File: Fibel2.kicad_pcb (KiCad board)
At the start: 2 copper layers, 210 x 148 mm, 315 parts, among them J1201 Orin Nano, J301 Conn_01x02, J302 Conn_01x02, J303 Conn_01x02, J702 SPK_JST_L, J703 SPK_JST_R, J704 Conn_02x20_Odd_Even, J801 Conn_02x20_Odd_Even, Q301 CSD17581Q3A, Q302 CSD17581Q3A, Q303 CSD17581Q3A, Q304 CSD17581Q3A, U1 TPS651851RSLT, U201 TLV75718PDBV, U202 TLV75733PDBV, U203 TPS61022RWUR, U204 TPS56428DDA, U301 BQ25798RQMR, U4 ESP32-S3-WROOM-1U, U402 TPS65988DHRSHR, U701 WM8960CGEFL

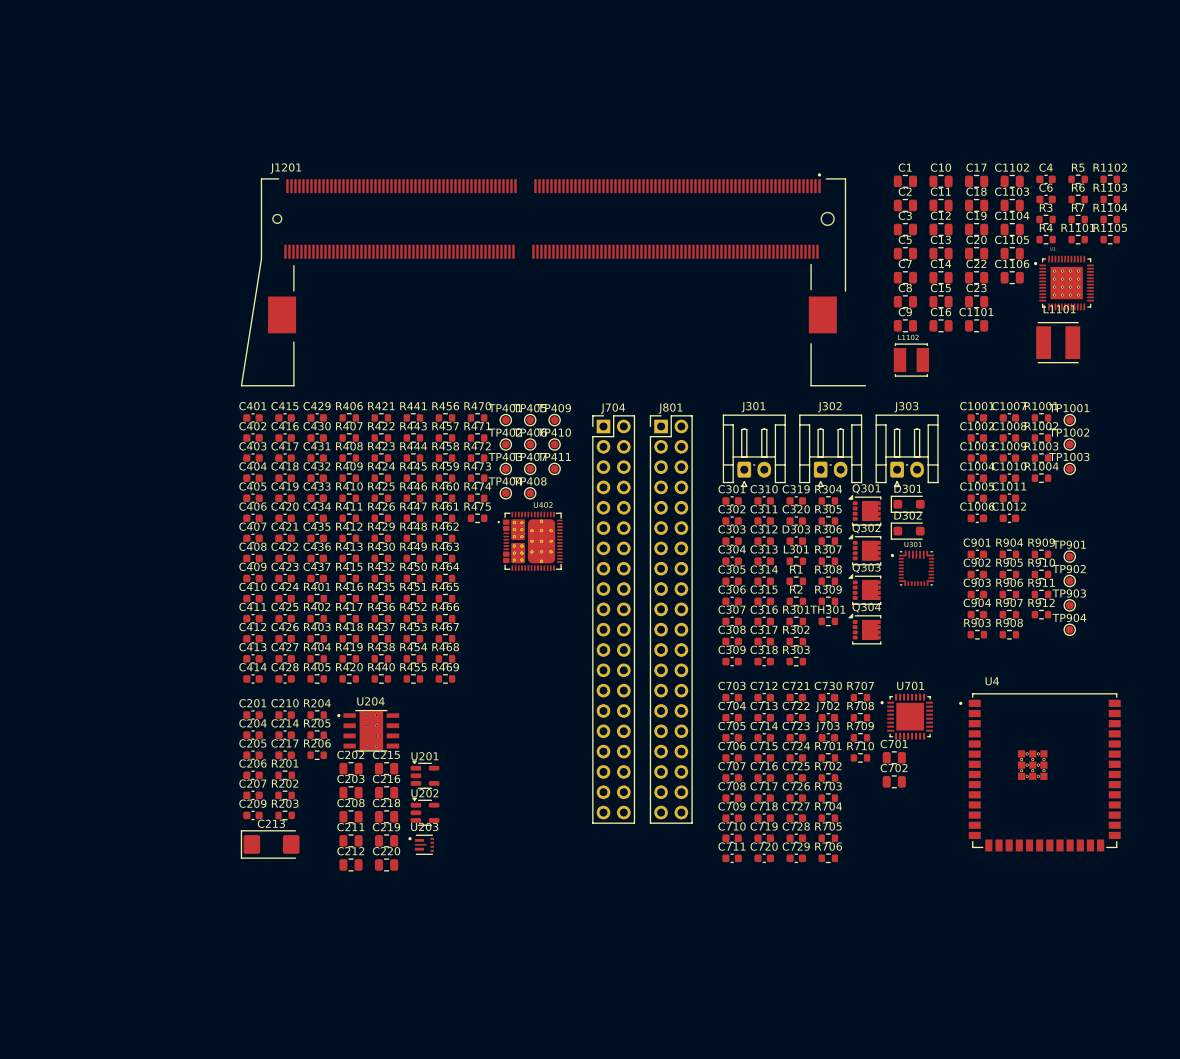
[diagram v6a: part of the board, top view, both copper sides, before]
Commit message: added some missing footprints, stared working ono power-on and sequencing
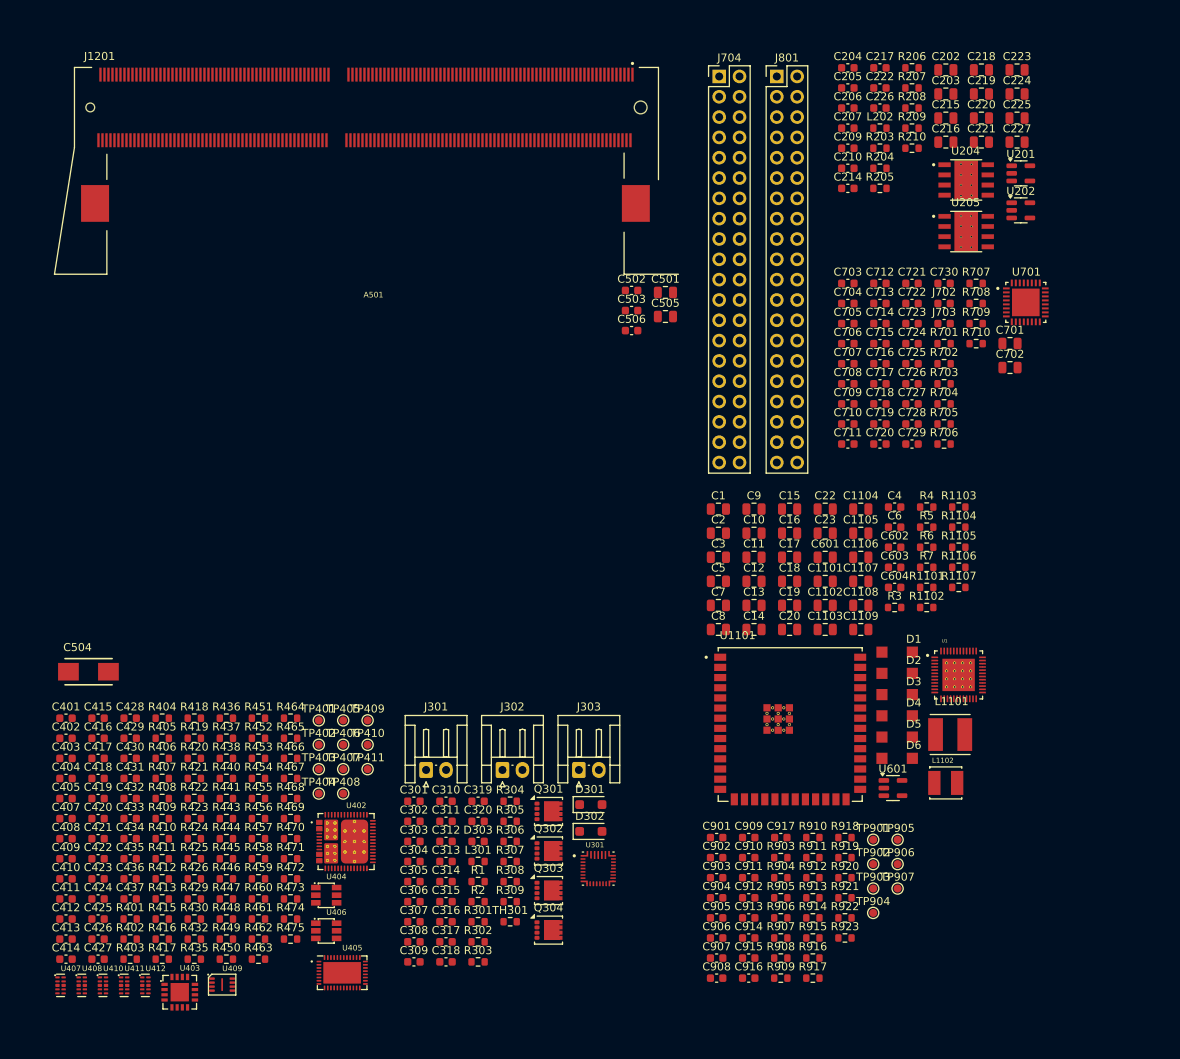
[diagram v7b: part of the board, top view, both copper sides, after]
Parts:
- removed C1001, C1002, C1003, C1004, C1005, C1006, C1007, C1008: 220nF, Capacitor_SMD:C_0603_1608Metric
- removed C1009, C1010, C1011, C1012: 20uF, Capacitor_SMD:C_0603_1608Metric
- removed C201: 10uF, Capacitor_SMD:C_0603_1608Metric
- removed C208, C211, C212: 22uF, Capacitor_SMD:C_0805_2012Metric
- removed C213: 330uF, Capacitor_Tantalum_SMD:CP_EIA-6032-15_Kemet-U
- removed C406: 10uF 25V, Capacitor_SMD:C_0603_1608Metric
- removed R1001, R1002: 47K, Resistor_SMD:R_0603_1608Metric
- removed R1003: 200R, Resistor_SMD:R_0603_1608Metric
- removed R1004: 0R 22A, Resistor_SMD:R_0603_1608Metric
- removed R201, R202: 100K, Resistor_SMD:R_0603_1608Metric
- removed TP1001, TP1002, TP1003: TP_0.75mm_SMD, TestPoint:TestPoint_Pad_D1.0mm
- removed U203: TPS61022RWUR, Fibel2:TPS61022RWUR
- removed U4: ESP32-S3-WROOM-1U, Fibel2:XCVR_ESP32-S3-WROOM-1U
- added A501: Jetson-Orin-NX-Nano, Fibel2:jetson-orin-nx-nano-module, F.Cu at (68.0, 57.0)
- added C1107: 10nF, Capacitor_SMD:C_0805_2012Metric, F.Cu at (130.2, 92.4)
- added C1108: 1uF, Capacitor_SMD:C_0805_2012Metric, F.Cu at (130.2, 95.4)
- added C1109: 22uF, Capacitor_SMD:C_0805_2012Metric, F.Cu at (130.2, 98.4)
- added C221: 22uF, Capacitor_SMD:C_0805_2012Metric, F.Cu at (145.2, 37.5)
- added C222: 10uF, Capacitor_SMD:C_0603_1608Metric, F.Cu at (132.6, 30.7)
- added C223: 0.1uF, Capacitor_SMD:C_0805_2012Metric, F.Cu at (149.7, 28.5)
- added C224: 22uF, Capacitor_SMD:C_0805_2012Metric, F.Cu at (149.7, 31.5)
- added C225: 22uF, Capacitor_SMD:C_0805_2012Metric, F.Cu at (149.7, 34.5)
- added C226: 22uF, Capacitor_SMD:C_0603_1608Metric, F.Cu at (132.6, 33.2)
- added C227: 22uF, Capacitor_SMD:C_0805_2012Metric, F.Cu at (149.7, 37.5)
- added C501: 22uF, Capacitor_SMD:C_0805_2012Metric, F.Cu at (105.7, 56.3)
- added C502: 10uF, Capacitor_SMD:C_0603_1608Metric, F.Cu at (101.5, 56.0)
- added C503: 1uF, Capacitor_SMD:C_0603_1608Metric, F.Cu at (101.5, 58.5)
- added C504: T495C107K006ATE150, Fibel2:CAPMP6032X250, F.Cu at (33.6, 103.7)
- added C505: 22uF, Capacitor_SMD:C_0805_2012Metric, F.Cu at (105.7, 59.3)
- added C506: 10uF, Capacitor_SMD:C_0603_1608Metric, F.Cu at (101.5, 61.1)
- added C601: 22uF, Capacitor_SMD:C_0805_2012Metric, F.Cu at (125.7, 89.4)
- added C602: 10uF, Capacitor_SMD:C_0603_1608Metric, F.Cu at (134.4, 88.1)
- added C603: 10uF, Capacitor_SMD:C_0603_1608Metric, F.Cu at (134.4, 90.7)
- added C604: 0.1uF, Capacitor_SMD:C_0603_1608Metric, F.Cu at (134.4, 93.2)
- added C905: 220nF, Capacitor_SMD:C_0603_1608Metric, F.Cu at (112.1, 134.5)
- added C906: 220nF, Capacitor_SMD:C_0603_1608Metric, F.Cu at (112.1, 137.0)
- added C907: 220nF, Capacitor_SMD:C_0603_1608Metric, F.Cu at (112.1, 139.5)
- added C908: 220nF, Capacitor_SMD:C_0603_1608Metric, F.Cu at (112.1, 142.0)
- added C909: 220nF, Capacitor_SMD:C_0603_1608Metric, F.Cu at (116.2, 124.4)
- added C910: 220nF, Capacitor_SMD:C_0603_1608Metric, F.Cu at (116.2, 126.9)
- added C911: 220nF, Capacitor_SMD:C_0603_1608Metric, F.Cu at (116.2, 129.4)
- added C912: 220nF, Capacitor_SMD:C_0603_1608Metric, F.Cu at (116.2, 132.0)
- added C913: 20uF, Capacitor_SMD:C_0603_1608Metric, F.Cu at (116.2, 134.5)
- added C914: 20uF, Capacitor_SMD:C_0603_1608Metric, F.Cu at (116.2, 137.0)
- added C915: 20uF, Capacitor_SMD:C_0603_1608Metric, F.Cu at (116.2, 139.5)
- added C916: 20uF, Capacitor_SMD:C_0603_1608Metric, F.Cu at (116.2, 142.0)
- added C917: 100nF, Capacitor_SMD:C_0603_1608Metric, F.Cu at (120.2, 124.4)
- added D1: MBR0540, Fibel2:SOD-123, F.Cu at (134.7, 101.3)
- added D2: MBR0540, Fibel2:SOD-123, F.Cu at (134.7, 103.9)
- added D3: MBR0540, Fibel2:SOD-123, F.Cu at (134.7, 106.6)
- added D4: MBR0540, Fibel2:SOD-123, F.Cu at (134.7, 109.2)
- added D5: MBR0540, Fibel2:SOD-123, F.Cu at (134.7, 111.9)
- added D6: MBR0540, Fibel2:SOD-123, F.Cu at (134.7, 114.5)
- added L202: 3.3uH, Resistor_SMD:R_0603_1608Metric, F.Cu at (132.6, 35.8)
- added R1106: 10K, Resistor_SMD:R_0603_1608Metric, F.Cu at (142.4, 90.7)
- added R1107: 10K, Resistor_SMD:R_0603_1608Metric, F.Cu at (142.4, 93.2)
- added R207: 365K, Resistor_SMD:R_0603_1608Metric, F.Cu at (136.6, 30.7)
- added R208: 49.9K, Resistor_SMD:R_0603_1608Metric, F.Cu at (136.6, 33.2)
- added R209: 100K, Resistor_SMD:R_0603_1608Metric, F.Cu at (136.6, 35.8)
- added R210: 10K, Resistor_SMD:R_0603_1608Metric, F.Cu at (136.6, 38.3)
- added R913: R_0R_0402, Resistor_SMD:R_0603_1608Metric, F.Cu at (124.2, 132.0)
- added R914: R_0R_0402, Resistor_SMD:R_0603_1608Metric, F.Cu at (124.2, 134.5)
- added R915: 47K, Resistor_SMD:R_0603_1608Metric, F.Cu at (124.2, 137.0)
- added R916: 47K, Resistor_SMD:R_0603_1608Metric, F.Cu at (124.2, 139.5)
- added R917: 200R, Resistor_SMD:R_0603_1608Metric, F.Cu at (124.2, 142.0)
- added R918: 0R 22A, Resistor_SMD:R_0603_1608Metric, F.Cu at (128.2, 124.4)
- added R919: R_0R_0402, Resistor_SMD:R_0603_1608Metric, F.Cu at (128.2, 126.9)
- added R920: R_0R_0402, Resistor_SMD:R_0603_1608Metric, F.Cu at (128.2, 129.4)
- added R921: R_0R_0402, Resistor_SMD:R_0603_1608Metric, F.Cu at (128.2, 132.0)
- added R922: R_0R_0402, Resistor_SMD:R_0603_1608Metric, F.Cu at (128.2, 134.5)
- added R923: R_0R_0402, Resistor_SMD:R_0603_1608Metric, F.Cu at (128.2, 137.0)
- added TP905: TP_0.75mm_SMD, TestPoint:TestPoint_Pad_D1.0mm, F.Cu at (134.8, 124.7)
- added TP906: TP_0.75mm_SMD, TestPoint:TestPoint_Pad_D1.0mm, F.Cu at (134.8, 127.8)
- added TP907: TP_0.75mm_SMD, TestPoint:TestPoint_Pad_D1.0mm, F.Cu at (134.8, 130.8)
- added U1101: ESP32-S3-WROOM-1U, Fibel2:XCVR_ESP32-S3-WROOM-1U, F.Cu at (121.3, 110.3)
- added U205: TPS56428DDA, Fibel2:TPS56428DDA, F.Cu at (143.3, 48.7)
- added U403: FT230X_QFN, Fibel2:QFN-16_1EP_4x4mm_P0.65mm, F.Cu at (45.0, 143.8)
- added U404: AP22615A_TSOT26, Fibel2:TSOT23-6, F.Cu at (63.3, 131.6)
- added U405: TUSB1046-DCIRNQ, Fibel2:WQFN-40_1EP_6x3mm_Pitch0.4mm_EP4.7x2.7mm, F.Cu at (65.3, 141.3)
- added U406: AP22615A_TSOT26, Fibel2:TSOT23-6, F.Cu at (63.3, 136.1)
- added U407: TPD4E05U06QDQARQ1, Fibel2:USON-10_2.5x1mm_P0.5mm, F.Cu at (30.1, 142.9)
- added U408: TPD4E05U06QDQARQ1, Fibel2:USON-10_2.5x1mm_P0.5mm, F.Cu at (32.8, 142.9)
- added U409: W25Q80DV_USON, Fibel2:USON-8_2x3mm_P0.5mm, F.Cu at (50.3, 142.8)
- added U410: TPD4E05U06QDQARQ1, Fibel2:USON-10_2.5x1mm_P0.5mm, F.Cu at (35.4, 142.9)
- added U411: TPD4E05U06QDQARQ1, Fibel2:USON-10_2.5x1mm_P0.5mm, F.Cu at (38.1, 142.9)
- added U412: TPD4E05U06QDQARQ1, Fibel2:USON-10_2.5x1mm_P0.5mm, F.Cu at (40.7, 142.9)
- added U601: TLV75733PDBV, Package_TO_SOT_SMD:SOT-23-5, F.Cu at (134.2, 118.2)
- C701, C702: value 100uF 10V -> 100uF
- C711, C712: value 680nF DNP -> 680nF
- moved C220 119.4 mm to (145.2, 34.5)
- moved C218 119.4 mm to (145.2, 28.5)
- moved C219 119.4 mm to (145.2, 31.5)
- moved C202 114.7 mm to (140.8, 28.5)
- moved C203 114.7 mm to (140.8, 31.5)
- moved C217 113.6 mm to (132.6, 28.2)
- moved R206 113.6 mm to (136.6, 28.2)
- moved C204 111.7 mm to (128.5, 28.2)
- moved C205 111.7 mm to (128.5, 30.7)
- moved C206 111.7 mm to (128.5, 33.2)
- moved C207 111.7 mm to (128.5, 35.8)
- moved C209 111.7 mm to (128.5, 38.3)
- moved R203 111.7 mm to (132.6, 38.3)
- moved C216 107.2 mm to (140.8, 37.5)
- moved C215 107.2 mm to (140.8, 34.5)
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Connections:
- net /Network/C_PCIE1_TX0_N renamed /PCIe/C_PCIE1_TX0_N
- net /Network/C_PCIE1_TX0_P renamed /PCIe/C_PCIE1_TX0_P
- net /Network/M2_E_I2C_CLK renamed /PCIe/M2_E_I2C_CLK
- net /Network/M2_E_I2C_DAT renamed /PCIe/M2_E_I2C_DAT
- net /Network/M2_E_SUSCLK renamed /PCIe/M2_E_SUSCLK
- net /Network/M2_E_W_DIS_1 renamed /PCIe/M2_E_W_DIS_1
- net /Network/M2_E_W_DIS_2 renamed /PCIe/M2_E_W_DIS_2
- net /Network/USB_E_N renamed /PCIe/USB_E_N
- net /Network/USB_E_P renamed /PCIe/USB_E_P
- net /Network/~{M2_E_ALERT} renamed /PCIe/~{M2_E_ALERT}
- net /Network/~{M2_E_UART_WAKE} renamed /PCIe/~{M2_E_UART_WAKE}
- C17 pad 1: Net-(C17-Pad1) -> Net-(U1-VEE_D)
- C205 pad 1: +3V3 -> PP3V3
- C207 pad 1: +3V3 -> PP3V3
- C210 pad 1: +3V3 -> PP3V3
- C309 pad 1: VSYS -> GND
- C312 pad 1: VSYS -> GND
- C315 pad 1: VSYS -> GND
- C317 pad 1: VSYS -> GND
- C319 pad 1: VSYS -> GND
- C320 pad 1: VSYS -> GND
- C404 pad 1: /USB/FTDI_3V3 -> +5V
- C407 pad 1: /USB/FTDI_3V3 -> +5V
- C408 pad 1: /USB/FTDI_3V3 -> +5V
- J1201 pad 103: UART0_TXD -> UART0_RTS
- J1201 pad 178: unconnected-(J1201C-MOD_SLEEP-Pad178) -> MOD_SLEEP
- J1201 pad 201: Net-(J1201D-GND-Pad201) -> GND
- J1201 pad 203: unconnected-(J1201D-UART1_TXD-Pad203) -> UART1_TXD
- J1201 pad 205: unconnected-(J1201D-UART1_RXD-Pad205) -> UART1_RXD
- J1201 pad 207: unconnected-(J1201D-UART1_RTS-Pad207) -> UART1_RTS
- J1201 pad 209: unconnected-(J1201D-UART1_CTS-Pad209) -> UART1_CTS
- J1201 pad 214: unconnected-(J1201D-FORCE_RECV-Pad214) -> RECOVERY
- J1201 pad 217: unconnected-(J1201D-MODULE_ID-Pad217) -> MOD_ID
- J1201 pad 231: Net-(J1201D-GND-Pad201) -> GND
- J1201 pad 233: unconnected-(J1201D-SHUTDOWN_REQ-Pad233) -> SHUTDOWN_REQ
- J1201 pad 235: unconnected-(J1201D-PMIC_BBAT-Pad235) -> PMIC_BBAT
- J1201 pad 237: unconnected-(J1201D-POWER_EN-Pad237) -> POWER_EN
- J1201 pad 239: unconnected-(J1201D-SYS_RESET-Pad239) -> SYS_RESET
- J1201 pad 240: unconnected-(J1201D-SLEEP/WAKE-Pad240) -> SLEEP/WAKE
- J1201 pad 241: Net-(J1201D-GND-Pad201) -> GND
- J1201 pad 242: Net-(J1201D-GND-Pad201) -> GND
- J1201 pad 243: Net-(J1201D-GND-Pad201) -> GND
- J1201 pad 244: Net-(J1201D-GND-Pad201) -> GND
- J1201 pad 245: Net-(J1201D-GND-Pad201) -> GND
- J1201 pad 246: Net-(J1201D-GND-Pad201) -> GND
- J1201 pad 247: Net-(J1201D-GND-Pad201) -> GND
- J1201 pad 248: Net-(J1201D-GND-Pad201) -> GND
- J1201 pad 249: Net-(J1201D-GND-Pad201) -> GND
- J1201 pad 250: Net-(J1201D-GND-Pad201) -> GND
- J1201 pad 99: UART0_RTS -> UART0_TXD
- R203 pad 2: /Power/B_EN -> /Power/CARRIER_EN
- R406 pad 1: /USB/FTDI_3V3 -> +5V
- R422 pad 2: /USB/FTDI_3V3 -> +5V
- R423 pad 2: /USB/FTDI_3V3 -> +5V
- R908 pad 2: /Network/32.7KHZ_OUT -> /PCIe/32.7KHZ_OUT
- U1 pad 23: /EPD/EPD_PWRGD -> /EPD/EPD_PGD
- U202 pad 3: /Power/CARRIER_EN -> +5V
- U202 pad 5: +3V3 -> PP3V3
- U301 pad 25: VSYS -> GND

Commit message: started arranging the components on the board, added some more missing footprints. starting to think about the overall distribution of parts
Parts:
- removed J704, J801: Conn_02x20_Odd_Even, Connector_PinHeader_2.54mm:PinHeader_2x20_P2.54mm_Vertical
- added ?: , , F.Cu at (51.5, 151.8)
- added ?: , , F.Cu at (51.5, 88.2)
- added J1: Raspi_Header, Fibel2:Raspberry_Bottom_Entry, F.Cu at (274.6, -47.2)
- added J2: Raspi_Header, Fibel2:Raspberry_Bottom_Entry, F.Cu at (50.2, 43.2)
- moved C428 282.8 mm to (321.3, 123.0)
- moved C429 282.8 mm to (321.3, 125.5)
- moved C430 282.8 mm to (321.3, 128.0)
- moved C431 282.8 mm to (321.3, 130.5)
- moved C432 282.8 mm to (321.3, 133.0)
- moved C433 282.8 mm to (321.3, 135.5)
- moved C434 282.8 mm to (321.3, 138.0)
- moved C435 282.8 mm to (321.3, 140.6)
- moved C436 282.8 mm to (321.3, 143.1)
- moved C437 282.8 mm to (321.3, 145.6)
- moved R401 282.8 mm to (321.3, 148.1)
- moved R402 282.8 mm to (321.3, 150.6)
- moved R403 282.8 mm to (321.3, 153.1)
- moved R404 282.8 mm to (325.3, 123.0)
- moved R405 282.8 mm to (325.3, 125.5)
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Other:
- board text added: "POWER"
- board text added: "USB"
